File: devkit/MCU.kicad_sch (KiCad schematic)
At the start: 38 parts, among them IC601 FAN5622SX, IC602 USBLC6-2P6, IC603 MX25U51245GZ4I00, IC604 NTS0104GU12, J601 Jumper, J602 Jumper, J603 Jumper, J604 Jumper, M601 NORA-B106, X601 DEBUG, X602 Current, X603 Device, X604 UART, X605 GPIO, X606 Current, X607 IO Current, X608 Display, X609 Current, X610 LED Current

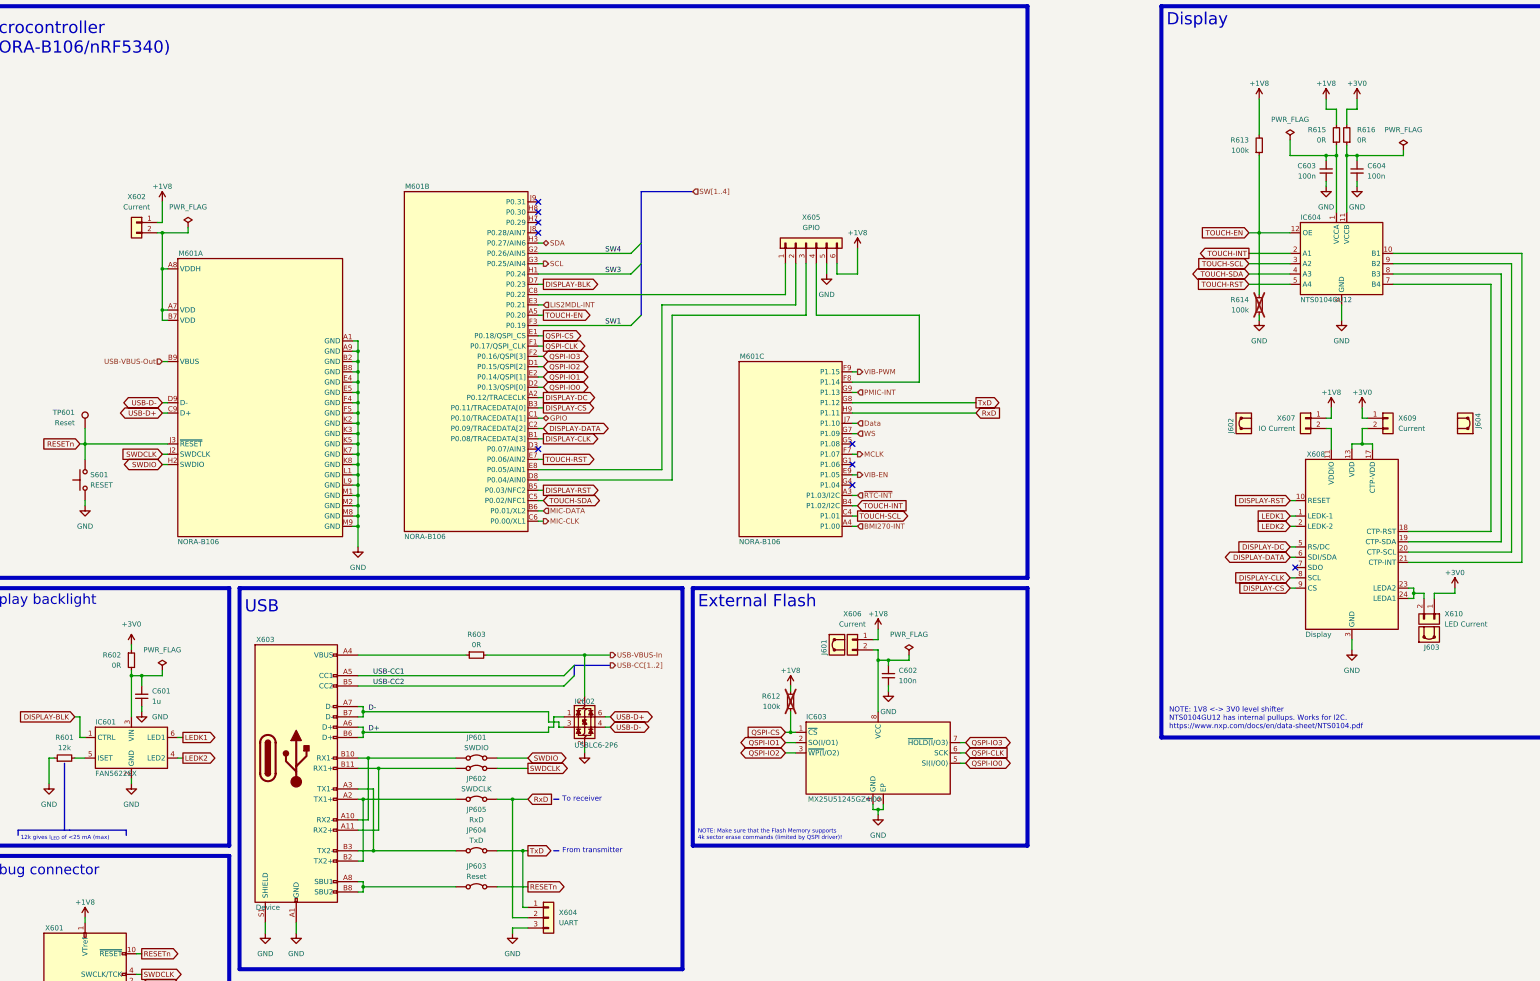
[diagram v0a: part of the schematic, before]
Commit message: Bug: Issue #198
- Change 3V0 to 3V3 to prevent flickering display

Closes: #198

Signed-off-by: Daniel Kampert <DanielKampert@kampis-elektroecke.de>
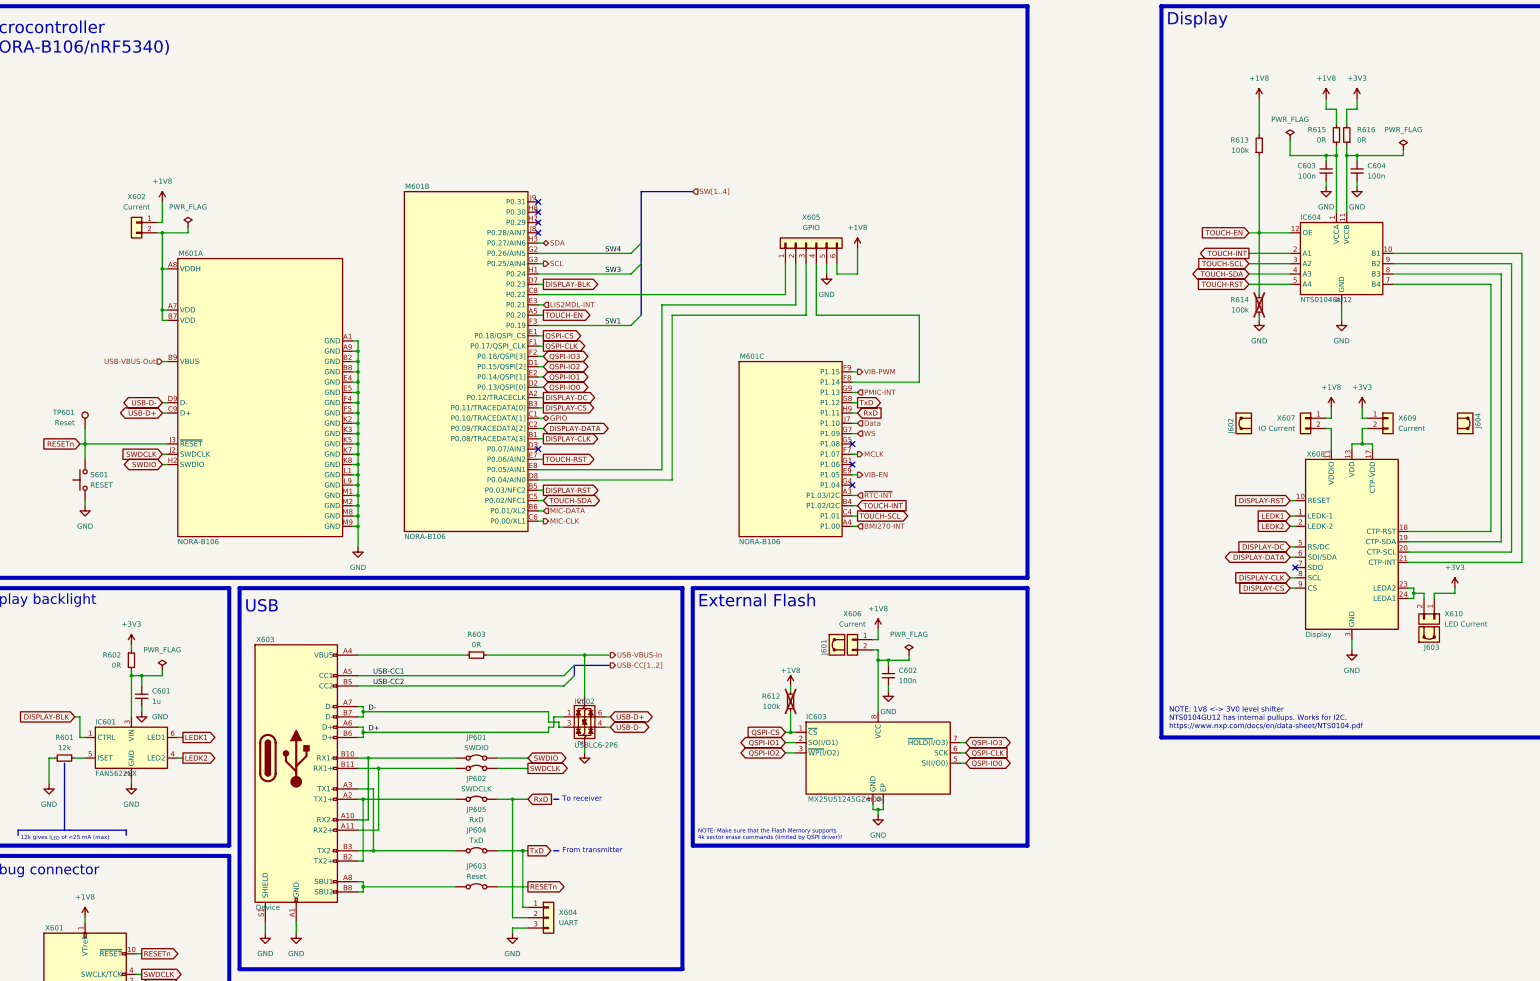
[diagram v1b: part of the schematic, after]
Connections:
- net +3V0 renamed +3V3
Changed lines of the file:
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@@
 	(wire
 		(pts
-			(xy 231.14 111.76) (xy 261.62 111.76)
+			(xy 231.14 111.76) (xy 232.41 111.76)
 		)
 		(stroke
@@
 	(wire
 		(pts
-			(xy 231.14 114.3) (xy 261.62 114.3)
+			(xy 231.14 114.3) (xy 232.41 114.3)
 		)
 		(stroke
@@
 	(global_label "RxD"
 		(shape input)
-		(at 261.62 114.3 0)
+		(at 232.41 114.3 0)
 		(fields_autoplaced yes)
 		(effects
@@
 		)
 		(property "Intersheetrefs" "${INTERSHEET_REFS}"
-			(at 268.1733 114.3 0)
+			(at 238.9633 114.3 0)
 			(effects
 				(font
@@
 	(global_label "TxD"
 		(shape output)
-		(at 261.62 111.76 0)
+		(at 232.41 111.76 0)
 		(fields_autoplaced yes)
 		(effects
@@
 		)
 		(property "Intersheetrefs" "${INTERSHEET_REFS}"
-			(at 267.8709 111.76 0)
+			(at 238.6609 111.76 0)
 			(effects
 				(font
@@
 		)
 		(property "Value" "+1V8"
-			(at 60.96 58.42 0)
+			(at 60.96 57.15 0)
 			(effects
 				(font
@@
 		)
 		(property "Value" "+1V8"
-			(at 232.41 69.85 0)
+			(at 232.41 68.58 0)
 			(effects
 				(font
@@
 		(on_board yes)
 		(dnp no)
+		(fields_autoplaced yes)
 		(property "Reference" "#PWR0603"
 			(at 41.91 242.57 0)
@@
 		)
 		(property "Value" "+1V8"
-			(at 41.91 234.95 0)
+			(at 41.91 233.68 0)
 			(effects
 				(font
@@
 		)
 		(property "Value" "+1V8"
-			(at 331.47 33.02 0)
+			(at 331.47 31.75 0)
 			(effects
 				(font
@@
 	)
 	(symbol
-		(lib_id "power:+3V0")
+		(lib_id "power:+3V3")
 		(at 379.73 157.48 0)
 		(unit 1)
@@
 			)
 		)
-		(property "Value" "+3V0"
-			(at 379.73 153.67 0)
+		(property "Value" "+3V3"
+			(at 379.73 152.4 0)
 			(effects
 				(font
@@
 			)
 		)
-		(property "Description" "Power symbol creates a global label with name \"+3V0\""
+		(property "Description" "Power symbol creates a global label with name \"+3V3\""
 			(at 379.73 157.48 0)
 			(effects
@@
 	)
 	(symbol
-		(lib_id "power:+3V0")
+		(lib_id "power:+3V3")
 		(at 53.34 171.45 0)
 		(unit 1)
@@
 			)
 		)
-		(property "Value" "+3V0"
+		(property "Value" "+3V3"
 			(at 53.34 166.37 0)
 			(effects
@@
 			)
 		)
-		(property "Description" "Power symbol creates a global label with name \"+3V0\""
+		(property "Description" "Power symbol creates a global label with name \"+3V3\""
 			(at 53.34 171.45 0)
 			(effects
@@
 	)
 	(symbol
-		(lib_id "power:+3V0")
+		(lib_id "power:+3V3")
 		(at 355.6 36.83 0)
 		(unit 1)
@@
 			)
 		)
-		(property "Value" "+3V0"
-			(at 355.6 33.02 0)
+		(property "Value" "+3V3"
+			(at 355.6 31.75 0)
 			(effects
 				(font
@@
 			)
 		)
-		(property "Description" "Power symbol creates a global label with name \"+3V0\""
+		(property "Description" "Power symbol creates a global label with name \"+3V3\""
 			(at 355.6 36.83 0)
 			(effects
@@
 		(on_board yes)
 		(dnp no)
+		(fields_autoplaced yes)
 		(property "Reference" "#PWR0625"
 			(at 349.25 116.84 0)
@@
 		)
 		(property "Value" "+1V8"
-			(at 349.25 109.22 0)
+			(at 349.25 107.95 0)
 			(effects
 				(font
@@
 		)
 		(property "Value" "+1V8"
-			(at 347.98 33.02 0)
+			(at 347.98 31.75 0)
 			(effects
 				(font
@@
 		)
 		(property "Value" "+1V8"
-			(at 237.49 163.83 0)
+			(at 237.49 162.56 0)
 			(effects
 				(font
@@
 	)
 	(symbol
-		(lib_id "power:+3V0")
+		(lib_id "power:+3V3")
 		(at 356.87 113.03 0)
 		(unit 1)
@@
 			)
 		)
-		(property "Value" "+3V0"
-			(at 356.87 109.22 0)
+		(property "Value" "+3V3"
+			(at 356.87 107.95 0)
 			(effects
 				(font
@@
 			)
 		)
-		(property "Description" "Power symbol creates a global label with name \"+3V0\""
+		(property "Description" "Power symbol creates a global label with name \"+3V3\""
 			(at 356.87 113.03 0)
 			(effects
